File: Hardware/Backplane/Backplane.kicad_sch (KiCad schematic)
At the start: 1 part, among them J101 10018784-10201TLF

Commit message: Adds more work on the backplane.
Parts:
- added C101, C102, C103, C104, C105, C106, C107, C108, C109, C110, C111, C112, C113, C114, C115, C116, C117, C118, C119, C120, C121, C122, C123, C124, C125, C126, C127, C128, C129, C130, C131, C132: 100n, symbol Device:C_Small
- added R101: 10K, symbol Device:R
- added SW101: SW_Push, symbol Switch:SW_Push
- added U101: P2X8C4M64P, Home Computer:QFP50P1600X1600X120-101N, symbol Home Computer:P2X8C4M64P
- added U102: TCA9548APWR, TCA9548APWR:SOP65P640X120-24N, symbol Home Computer:TCA9548APWR
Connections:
- net +3V3: now also C117.1, C118.1, C119.1, C120.1, C121.1, C122.1, C123.1, C124.1, C125.1, C126.1, C127.1, C128.1, C129.1, C130.1, C131.1, C132.1, R101.1, U101.11 (V0407), U101.17 (V0811), U101.23 (V1215), U101.29 (V1619), U101.35 (V2023), U101.41 (V2427), U101.47 (V2831), U101.5 (V0003), U101.55 (V3235), U101.61 (V3639), U101.67 (V4043), U101.73 (V4447), U101.79 (V4851), U101.85 (V5255), U101.91 (V5659), U101.97 (V6063)
- net CLK_{16MHz}: now also U101.51 (XI)
- net FAB_{0}: now also U101.89 (P56)
- net FAB_{1}: now also U101.90 (P57)
- net FAB_{2}: now also U101.92 (P58)
- net FAB_{3}: now also U101.93 (P59)
- net FAB_{4}: now also U101.95 (P60)
- net FAB_{5}: now also U101.96 (P61)
- net FAB_{6}: now also U101.98 (P62)
- net FAB_{7}: now also U101.99 (P63)
- net GND: now also C101.2, C102.2, C103.2, C104.2, C105.2, C106.2, C107.2, C108.2, C109.2, C110.2, C111.2, C112.2, C113.2, C114.2, C115.2, C116.2, C117.2, C118.2, C119.2, C120.2, C121.2, C122.2, C123.2, C124.2, C125.2, C126.2, C127.2, C128.2, C129.2, C130.2, C131.2, C132.2, SW101.1, U101.1 (TEST), U101.101 (GND)
- net MOD1_{GP0}: now also U101.3 (P0)
- net MOD1_{GP1}: now also U101.4 (P1)
- net MOD1_{GP2}: now also U101.6 (P2)
- net MOD1_{GP3}: now also U101.7 (P3)
- net MOD1_{GP4}: now also U101.9 (P4)
- net MOD1_{GP5}: now also U101.10 (P5)
- net MOD1_{GP6}: now also U101.12 (P6)
- net MOD1_{GP7}: now also U101.13 (P7)
- net MOD2_{GP0}: now also U101.15 (P8)
- net MOD2_{GP1}: now also U101.16 (P9)
- net MOD2_{GP2}: now also U101.18 (P10)
- net MOD2_{GP3}: now also U101.19 (P11)
- net MOD2_{GP4}: now also U101.21 (P12)
- net MOD2_{GP5}: now also U101.22 (P13)
- net MOD2_{GP6}: now also U101.24 (P14)
- net MOD2_{GP7}: now also U101.25 (P15)
- net MOD3_{GP0}: now also U101.27 (P16)
- net MOD3_{GP1}: now also U101.28 (P17)
- net MOD3_{GP2}: now also U101.30 (P18)
- net MOD3_{GP3}: now also U101.31 (P19)
- net MOD3_{GP4}: now also U101.33 (P20)
- net MOD3_{GP5}: now also U101.34 (P21)
- net MOD3_{GP6}: now also U101.36 (P22)
- net MOD3_{GP7}: now also U101.37 (P23)
- net MOD4_{GP0}: now also U101.39 (P24)
- net MOD4_{GP1}: now also U101.40 (P25)
- net MOD4_{GP2}: now also U101.42 (P26)
- net MOD4_{GP3}: now also U101.43 (P27)
- net MOD4_{GP4}: now also U101.45 (P28)
- net MOD4_{GP5}: now also U101.46 (P29)
- net MOD4_{GP6}: now also U101.48 (P30)
- net MOD4_{GP7}: now also U101.49 (P31)
- net MOD5_{GP0}: now also U101.53 (P32)
- net MOD5_{GP1}: now also U101.54 (P33)
- net MOD5_{GP2}: now also U101.56 (P34)
- net MOD5_{GP3}: now also U101.57 (P35)
- net MOD5_{GP4}: now also U101.59 (P36)
- net MOD5_{GP5}: now also U101.60 (P37)
- net MOD5_{GP6}: now also U101.62 (P38)
- net MOD5_{GP7}: now also U101.63 (P39)
- net MOD6_{GP0}: now also U101.65 (P40)
- net MOD6_{GP1}: now also U101.66 (P41)
- net MOD6_{GP2}: now also U101.68 (P42)
- net MOD6_{GP3}: now also U101.69 (P43)
- net MOD6_{GP4}: now also U101.71 (P44)
- net MOD6_{GP5}: now also U101.72 (P45)
- net MOD6_{GP6}: now also U101.74 (P46)
- net MOD6_{GP7}: now also U101.75 (P47)
- net MOD7_{GP0}: now also U101.77 (P48)
- net MOD7_{GP1}: now also U101.78 (P49)
- net MOD7_{GP2}: now also U101.80 (P50)
- net MOD7_{GP3}: now also U101.81 (P51)
- net MOD7_{GP4}: now also U101.83 (P52)
- net MOD7_{GP5}: now also U101.84 (P53)
- net MOD7_{GP6}: now also U101.86 (P54)
- net MOD7_{GP7}: now also U101.87 (P55)
- new net +1V8: C101.1, C102.1, C103.1, C104.1, C105.1, C106.1, C107.1, C108.1, C109.1, C110.1, C111.1, C112.1, C113.1, C114.1, C115.1, C116.1, U101.14 (VDD), U101.2 (VDD), U101.20 (VDD), U101.26 (VDD), U101.32 (VDD), U101.38 (VDD), U101.44 (VDD), U101.52 (VDD), U101.58 (VDD), U101.64 (VDD), U101.70 (VDD), U101.76 (VDD), U101.8 (VDD), U101.82 (VDD), U101.88 (VDD), U101.94 (VDD)
- new net ~{RESET}: R101.2, SW101.2, U101.100 (~{RES})
- no-connect marks 0 -> 1

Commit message: snapshot before refactor
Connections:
- net +5V: now also U102.24 (VCC)
- net GND: now also U102.1 (A0), U102.12 (GND), U102.2 (A1), U102.21 (A2)
- net ~{RESET}: now also U102.3 (~{RESET})
- net I2C_{SCL}: now reaches J101.A27 (I2C_{SCL})
- net I2C_{SCL}: now also U102.22 (SCL)
- net I2C_{SDA}: now reaches J101.A28 (I2C_{SDA})
- net I2C_{SDA}: now also U102.23 (SDA)

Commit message: Improves Backplane Schematic a lot
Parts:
- removed C101, C102, C103, C104, C105, C106, C107, C108, C109, C110, C111, C112, C113, C114, C115, C116, C117, C118, C119, C120, C121, C122, C123, C124, C125, C126, C127, C128, C129, C130, C131, C132: 100n, symbol Device:C_Small
- removed J101: 10018784-10201TLF, Home Computer:CONN_10018784-10201TLF, symbol Home Computer:AHC-CORECONN-GEN1 Socket
- removed R101: 10K, symbol Device:R
- removed SW101: SW_Push, symbol Switch:SW_Push
- removed unit 2 of U101
- added C101, C102, C103: 100n, Capacitor_SMD:C_0603_1608Metric, symbol Device:C
- added TP101, TP102, TP103, TP104: TestPoint, TestPoint:TestPoint_Pad_D1.5mm, symbol Connector:TestPoint
- added U103, U104: MCP23017_SO, Package_SO:SOIC-28W_7.5x17.9mm_P1.27mm, symbol Interface_Expansion:MCP23017_SO
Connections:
- net +3V3: now also C101.2, C102.2, C103.2, U103.9 (VDD), U104.15 (A0), U104.9 (VDD)
- net GND: now also C101.1, C102.1, C103.1, U103.10 (VSS), U103.15 (A0), U103.16 (A1), U103.17 (A2), U104.10 (VSS), U104.16 (A1), U104.17 (A2)
- net I2C1_{SCL}: now also U102.7 (SC1)
- net I2C1_{SDA}: now also U102.6 (SD1)
- net I2C2_{SCL}: now also U102.9 (SC2)
- net I2C2_{SDA}: now also U102.8 (SD2)
- net I2C3_{SCL}: now also U102.11 (SC3)
- net I2C3_{SDA}: now also U102.10 (SD3)
- net I2C4_{SCL}: now also U102.14 (SC4)
- net I2C4_{SDA}: now also U102.13 (SD4)
- net I2C5_{SCL}: now also U102.16 (SC5)
- net I2C5_{SDA}: now also U102.15 (SD5)
- net I2C6_{SCL}: now also U102.18 (SC6)
- net I2C6_{SDA}: now also U102.17 (SD6)
- net I2C7_{SCL}: now also U102.20 (SC7)
- net I2C7_{SDA}: now also U102.19 (SD7)
- net ~{RESET}: now also U103.18 (~{RESET}), U104.18 (~{RESET}); no longer U101.100 (~{RES})
- net I2C^{BRD}_{SCL}: now reaches U102.4 (SD0)
- net I2C^{BRD}_{SCL}: now also U103.12 (SCK), U104.12 (SCK)
- net I2C^{BRD}_{SDA}: now reaches U102.5 (SC0)
- net I2C^{BRD}_{SDA}: now also U103.13 (SDA), U104.13 (SDA)
- net CLK_{16MHz} renamed CLOCK
- net I2C_{SCL} renamed I2C^{FAB}_{SCL}
- net I2C_{SDA} renamed I2C^{FAB}_{SDA}
- new net: TP101.1, U103.19 (INTB)
- new net: TP102.1, U103.20 (INTA)
- new net: TP103.1, U104.19 (INTB)
- new net CLOCK_{DIV0}: U104.1 (GPB0)
- new net CLOCK_{DIV1}: U104.2 (GPB1)
- new net CLOCK_{DIV2}: U104.3 (GPB2)
- new net EXP_{~{IRQ}}: TP104.1, U104.20 (INTA)
- new net MOD^{1}_{~{IRQ}}: U103.2 (GPB1)
- new net MOD^{1}_{~{PDET}}: U103.22 (GPA1)
- new net MOD^{1}_{~{RESET}}: U104.22 (GPA1)
- new net MOD^{2}_{~{IRQ}}: U103.3 (GPB2)
- new net MOD^{2}_{~{PDET}}: U103.23 (GPA2)
- new net MOD^{2}_{~{RESET}}: U104.23 (GPA2)
- new net MOD^{3}_{~{IRQ}}: U103.4 (GPB3)
- new net MOD^{3}_{~{PDET}}: U103.24 (GPA3)
- new net MOD^{3}_{~{RESET}}: U104.24 (GPA3)
- new net MOD^{4}_{~{IRQ}}: U103.5 (GPB4)
- new net MOD^{4}_{~{PDET}}: U103.25 (GPA4)
- new net MOD^{4}_{~{RESET}}: U104.25 (GPA4)
- new net MOD^{5}_{~{IRQ}}: U103.6 (GPB5)
- new net MOD^{5}_{~{PDET}}: U103.26 (GPA5)
- new net MOD^{5}_{~{RESET}}: U104.26 (GPA5)
- new net MOD^{6}_{~{IRQ}}: U103.7 (GPB6)
- new net MOD^{6}_{~{PDET}}: U103.27 (GPA6)
- new net MOD^{6}_{~{RESET}}: U104.27 (GPA6)
- new net MOD^{7}_{~{IRQ}}: U103.8 (GPB7)
- new net MOD^{7}_{~{PDET}}: U103.28 (GPA7)
- new net MOD^{7}_{~{RESET}}: U104.28 (GPA7)
- new net Reset Gate/~{OUT}: U101.100 (~{RES})
- no-connect marks 1 -> 10
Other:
- added sheet Builtins (builtins.kicad_sch)
- added sheet Power (power.kicad_sch)
- added sheet Reset Gate (reset_gate.kicad_sch)
- sheet Module Slot 1 ports: added I2S_{WCLK}, SLOT_{AUDIO}, SLOT_{PRESENT}, SLOT_{VIDEO}, ~{RESET}; removed I2S_{LRCLK}
- sheet Module Slot 2 ports: added I2S_{WCLK}, SLOT_{AUDIO}, SLOT_{PRESENT}, SLOT_{VIDEO}, ~{RESET}; removed I2S_{LRCLK}
- sheet Module Slot 3 ports: added I2S_{WCLK}, SLOT_{AUDIO}, SLOT_{PRESENT}, SLOT_{VIDEO}, ~{RESET}; removed I2S_{LRCLK}
- sheet Module Slot 4 ports: added I2S_{WCLK}, SLOT_{AUDIO}, SLOT_{PRESENT}, SLOT_{VIDEO}, ~{RESET}; removed I2S_{LRCLK}
- sheet Module Slot 5 ports: added I2S_{WCLK}, SLOT_{AUDIO}, SLOT_{PRESENT}, SLOT_{VIDEO}, ~{RESET}; removed I2S_{LRCLK}
- sheet Module Slot 6 ports: added I2S_{WCLK}, SLOT_{AUDIO}, SLOT_{PRESENT}, SLOT_{VIDEO}, ~{RESET}; removed I2S_{LRCLK}
- sheet Module Slot 7 ports: added I2S_{WCLK}, SLOT_{AUDIO}, SLOT_{PRESENT}, SLOT_{VIDEO}, ~{RESET}; removed I2S_{LRCLK}
- moved on the sheet: U101A, U102

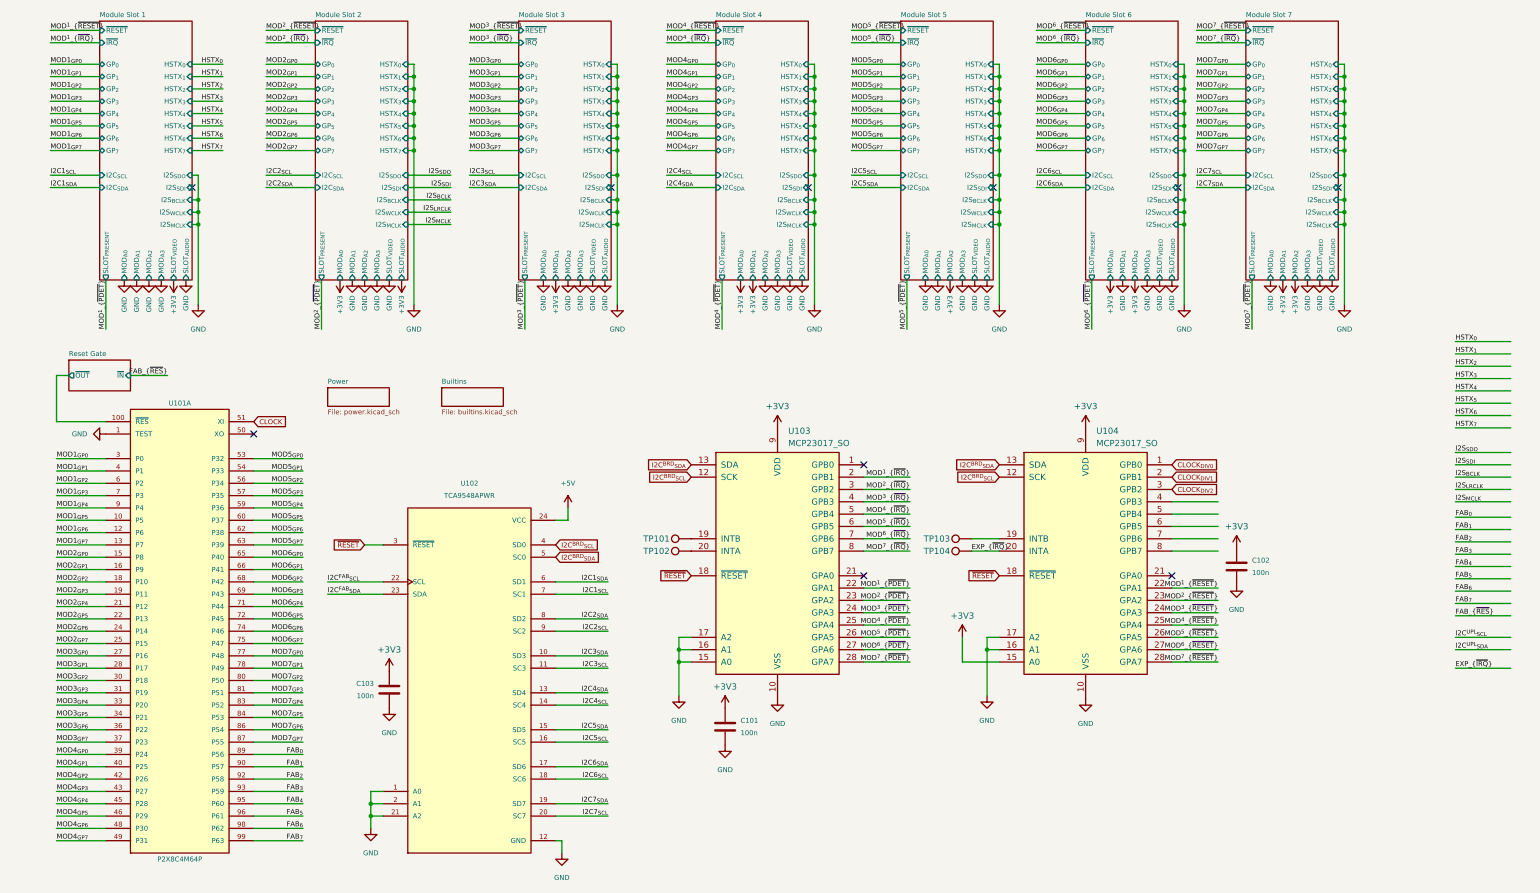
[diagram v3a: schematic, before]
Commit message: Some work on the backplane schematics: Improves module locality
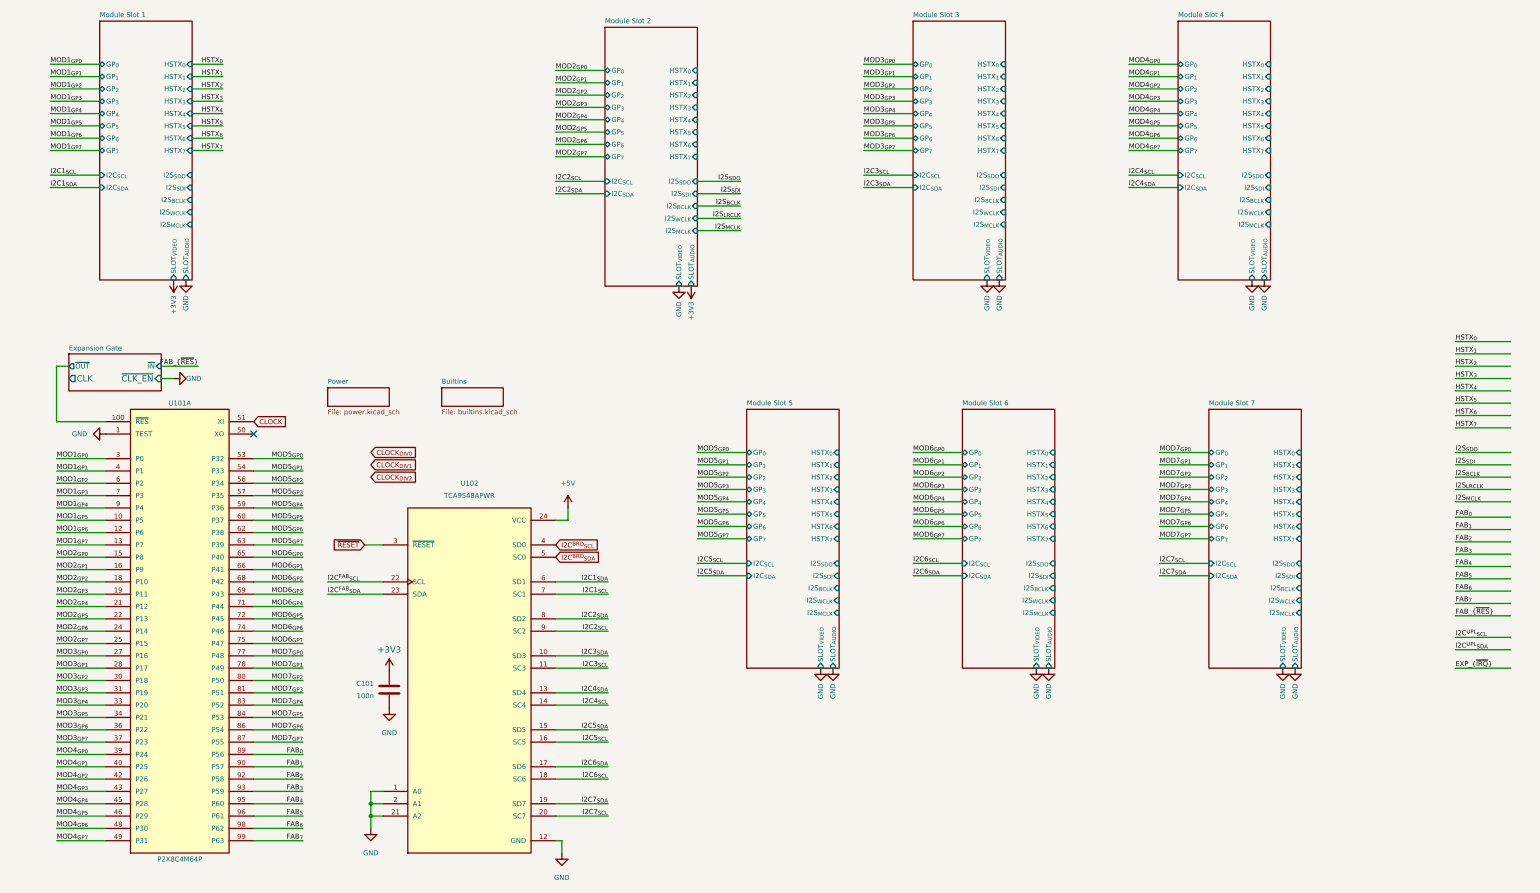
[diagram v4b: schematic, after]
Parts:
- removed C101, C102: 100n, Capacitor_SMD:C_0603_1608Metric, symbol Device:C
- removed TP101, TP102, TP103, TP104: TestPoint, TestPoint:TestPoint_Pad_D1.5mm, symbol Connector:TestPoint
- removed U103, U104: MCP23017_SO, Package_SO:SOIC-28W_7.5x17.9mm_P1.27mm, symbol Interface_Expansion:MCP23017_SO
- renumbered C103 to C101
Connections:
- no-connect marks 10 -> 1
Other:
- sheet Reset Gate renamed Expansion Gate
- sheet Expansion Gate ports: added CLK, ~{CLK_EN}; removed none
- sheet Module Slot 1 ports: added none; removed MOD_{A0}, MOD_{A1}, MOD_{A2}, MOD_{A3}, SLOT_{PRESENT}, ~{IRQ}, ~{RESET}
- sheet Module Slot 2 ports: added none; removed MOD_{A0}, MOD_{A1}, MOD_{A2}, MOD_{A3}, SLOT_{PRESENT}, ~{IRQ}, ~{RESET}
- sheet Module Slot 3 ports: added none; removed MOD_{A0}, MOD_{A1}, MOD_{A2}, MOD_{A3}, SLOT_{PRESENT}, ~{IRQ}, ~{RESET}
- sheet Module Slot 4 ports: added none; removed MOD_{A0}, MOD_{A1}, MOD_{A2}, MOD_{A3}, SLOT_{PRESENT}, ~{IRQ}, ~{RESET}
- sheet Module Slot 5 ports: added none; removed MOD_{A0}, MOD_{A1}, MOD_{A2}, MOD_{A3}, SLOT_{PRESENT}, ~{IRQ}, ~{RESET}
- sheet Module Slot 6 ports: added none; removed MOD_{A0}, MOD_{A1}, MOD_{A2}, MOD_{A3}, SLOT_{PRESENT}, ~{IRQ}, ~{RESET}
- sheet Module Slot 7 ports: added none; removed MOD_{A0}, MOD_{A1}, MOD_{A2}, MOD_{A3}, SLOT_{PRESENT}, ~{IRQ}, ~{RESET}

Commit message: Starts to implement a tool to generate symbols for KiCAD from a generic description.
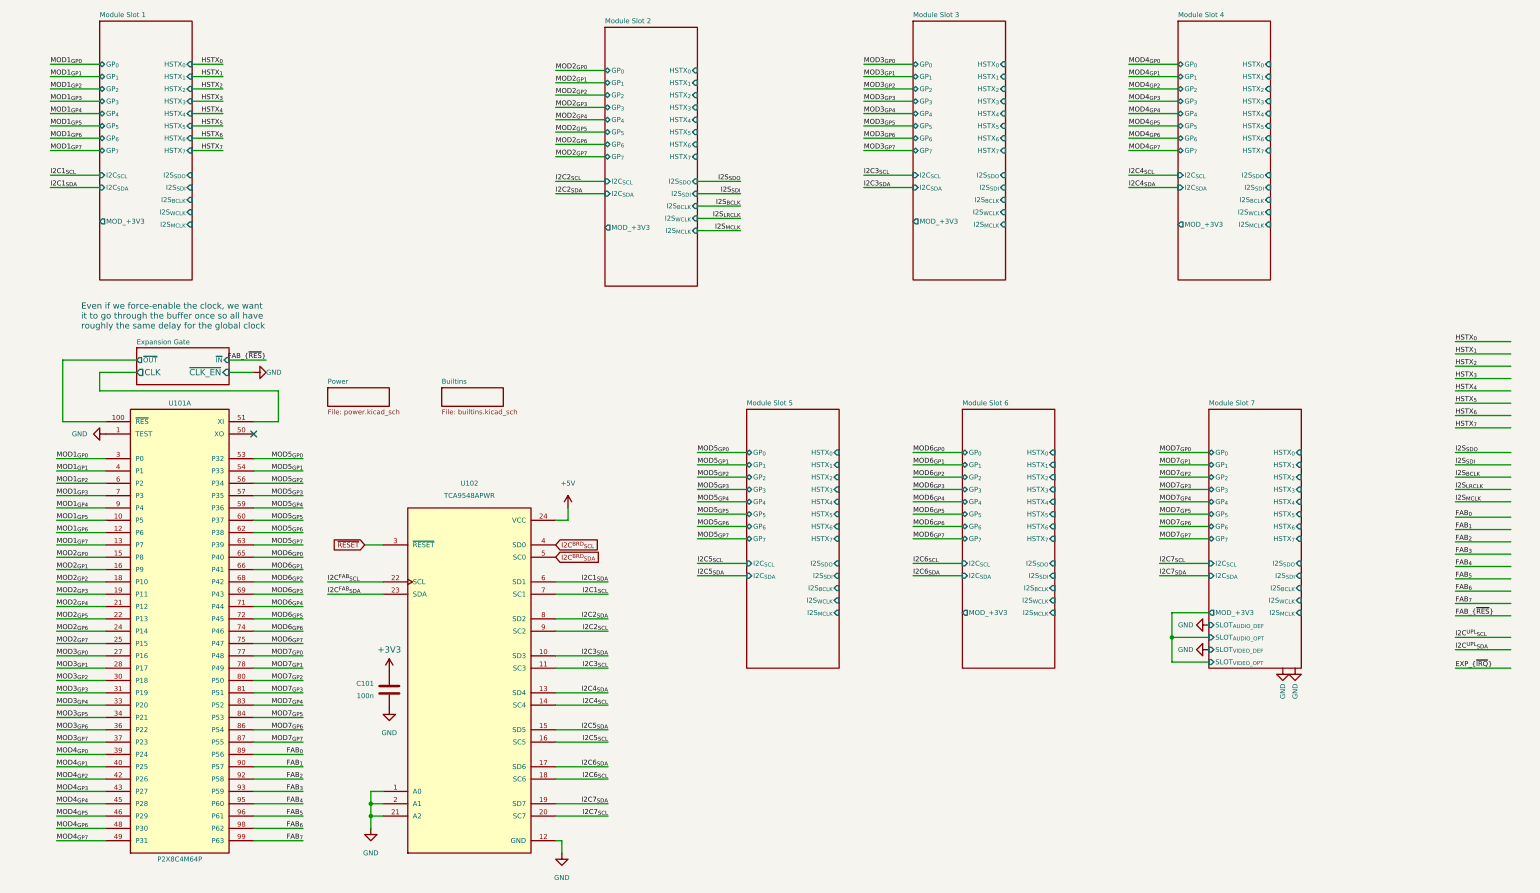
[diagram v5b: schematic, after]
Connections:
- net CLOCK is gone; now on net Expansion Gate/CLK: U101.51 (XI)
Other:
- sheet Module Slot 1 ports: added MOD_+3V3; removed SLOT_{AUDIO}, SLOT_{VIDEO}
- sheet Module Slot 2 ports: added MOD_+3V3; removed SLOT_{AUDIO}, SLOT_{VIDEO}
- sheet Module Slot 3 ports: added MOD_+3V3; removed SLOT_{AUDIO}, SLOT_{VIDEO}
- sheet Module Slot 4 ports: added MOD_+3V3; removed SLOT_{AUDIO}, SLOT_{VIDEO}
- sheet Module Slot 5 ports: added none; removed SLOT_{AUDIO}, SLOT_{VIDEO}
- sheet Module Slot 6 ports: added MOD_+3V3; removed SLOT_{AUDIO}, SLOT_{VIDEO}
- sheet Module Slot 7 ports: added MOD_+3V3, SLOT_{AUDIO_DEF}, SLOT_{AUDIO_OPT}, SLOT_{VIDEO_DEF}, SLOT_{VIDEO_OPT}; removed SLOT_{AUDIO}, SLOT_{VIDEO}
- note added: "Even if we force-enable the clock, we want it to go through the buffer once so all have roughly the same delay for the global clock"

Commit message: Cleans up the backplane schematic and improves on features a lot.
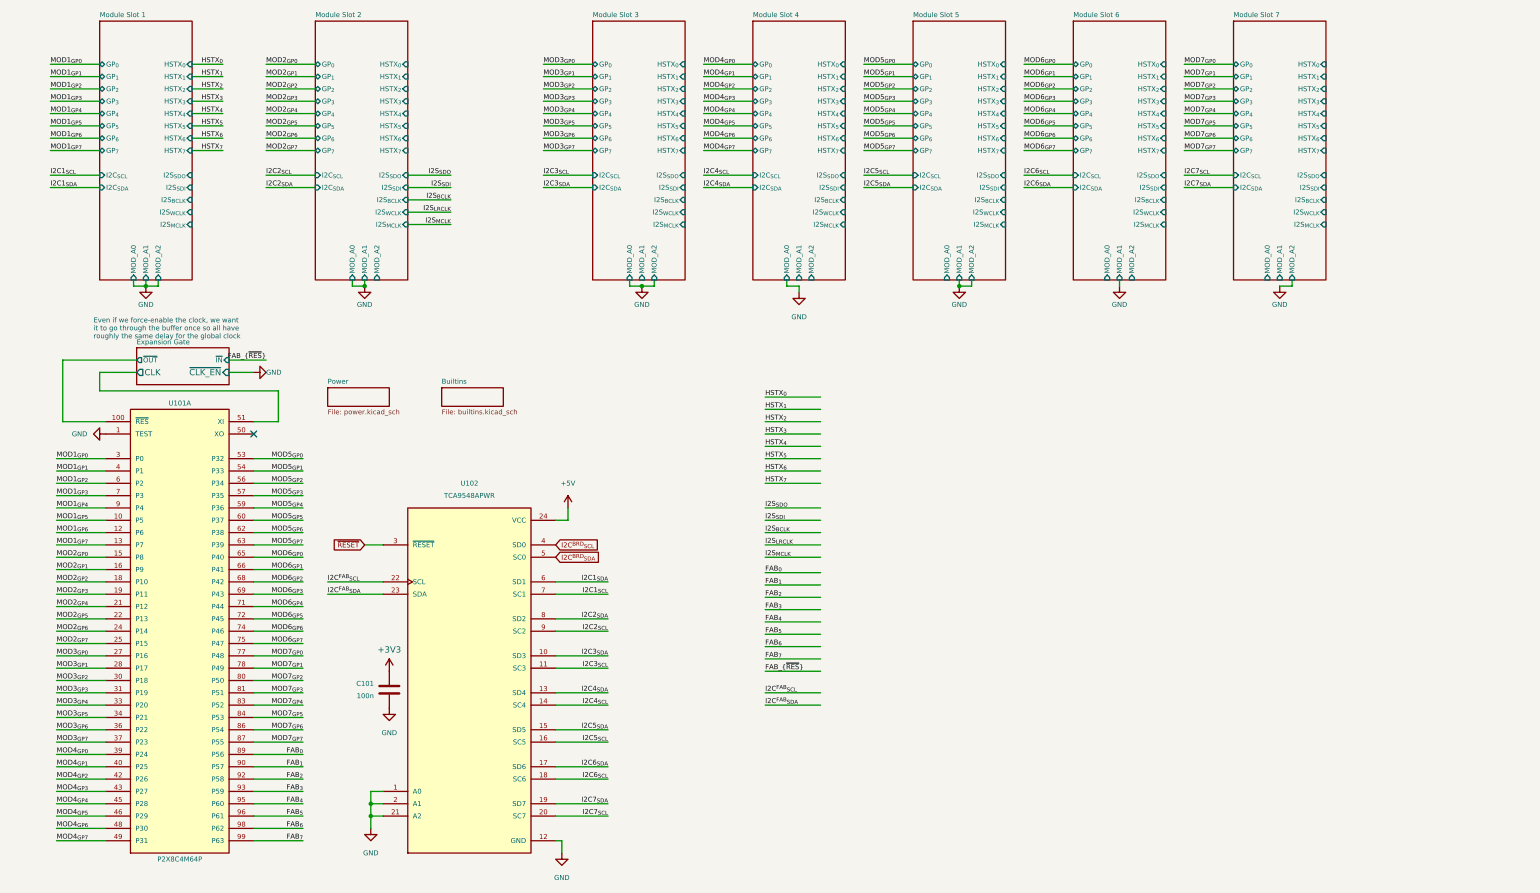
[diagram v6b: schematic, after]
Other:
- sheet Module Slot 1 ports: added MOD_A0, MOD_A1, MOD_A2; removed MOD_+3V3
- sheet Module Slot 2 ports: added MOD_A0, MOD_A1, MOD_A2; removed MOD_+3V3
- sheet Module Slot 3 ports: added MOD_A0, MOD_A1, MOD_A2; removed MOD_+3V3
- sheet Module Slot 4 ports: added MOD_A0, MOD_A1, MOD_A2; removed MOD_+3V3
- sheet Module Slot 5 ports: added MOD_A0, MOD_A1, MOD_A2; removed none
- sheet Module Slot 6 ports: added MOD_A0, MOD_A1, MOD_A2; removed MOD_+3V3
- sheet Module Slot 7 ports: added MOD_A0, MOD_A1, MOD_A2; removed MOD_+3V3, SLOT_{AUDIO_DEF}, SLOT_{AUDIO_OPT}, SLOT_{VIDEO_DEF}, SLOT_{VIDEO_OPT}
